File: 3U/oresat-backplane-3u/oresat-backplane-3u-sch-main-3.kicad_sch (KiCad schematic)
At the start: 30 parts

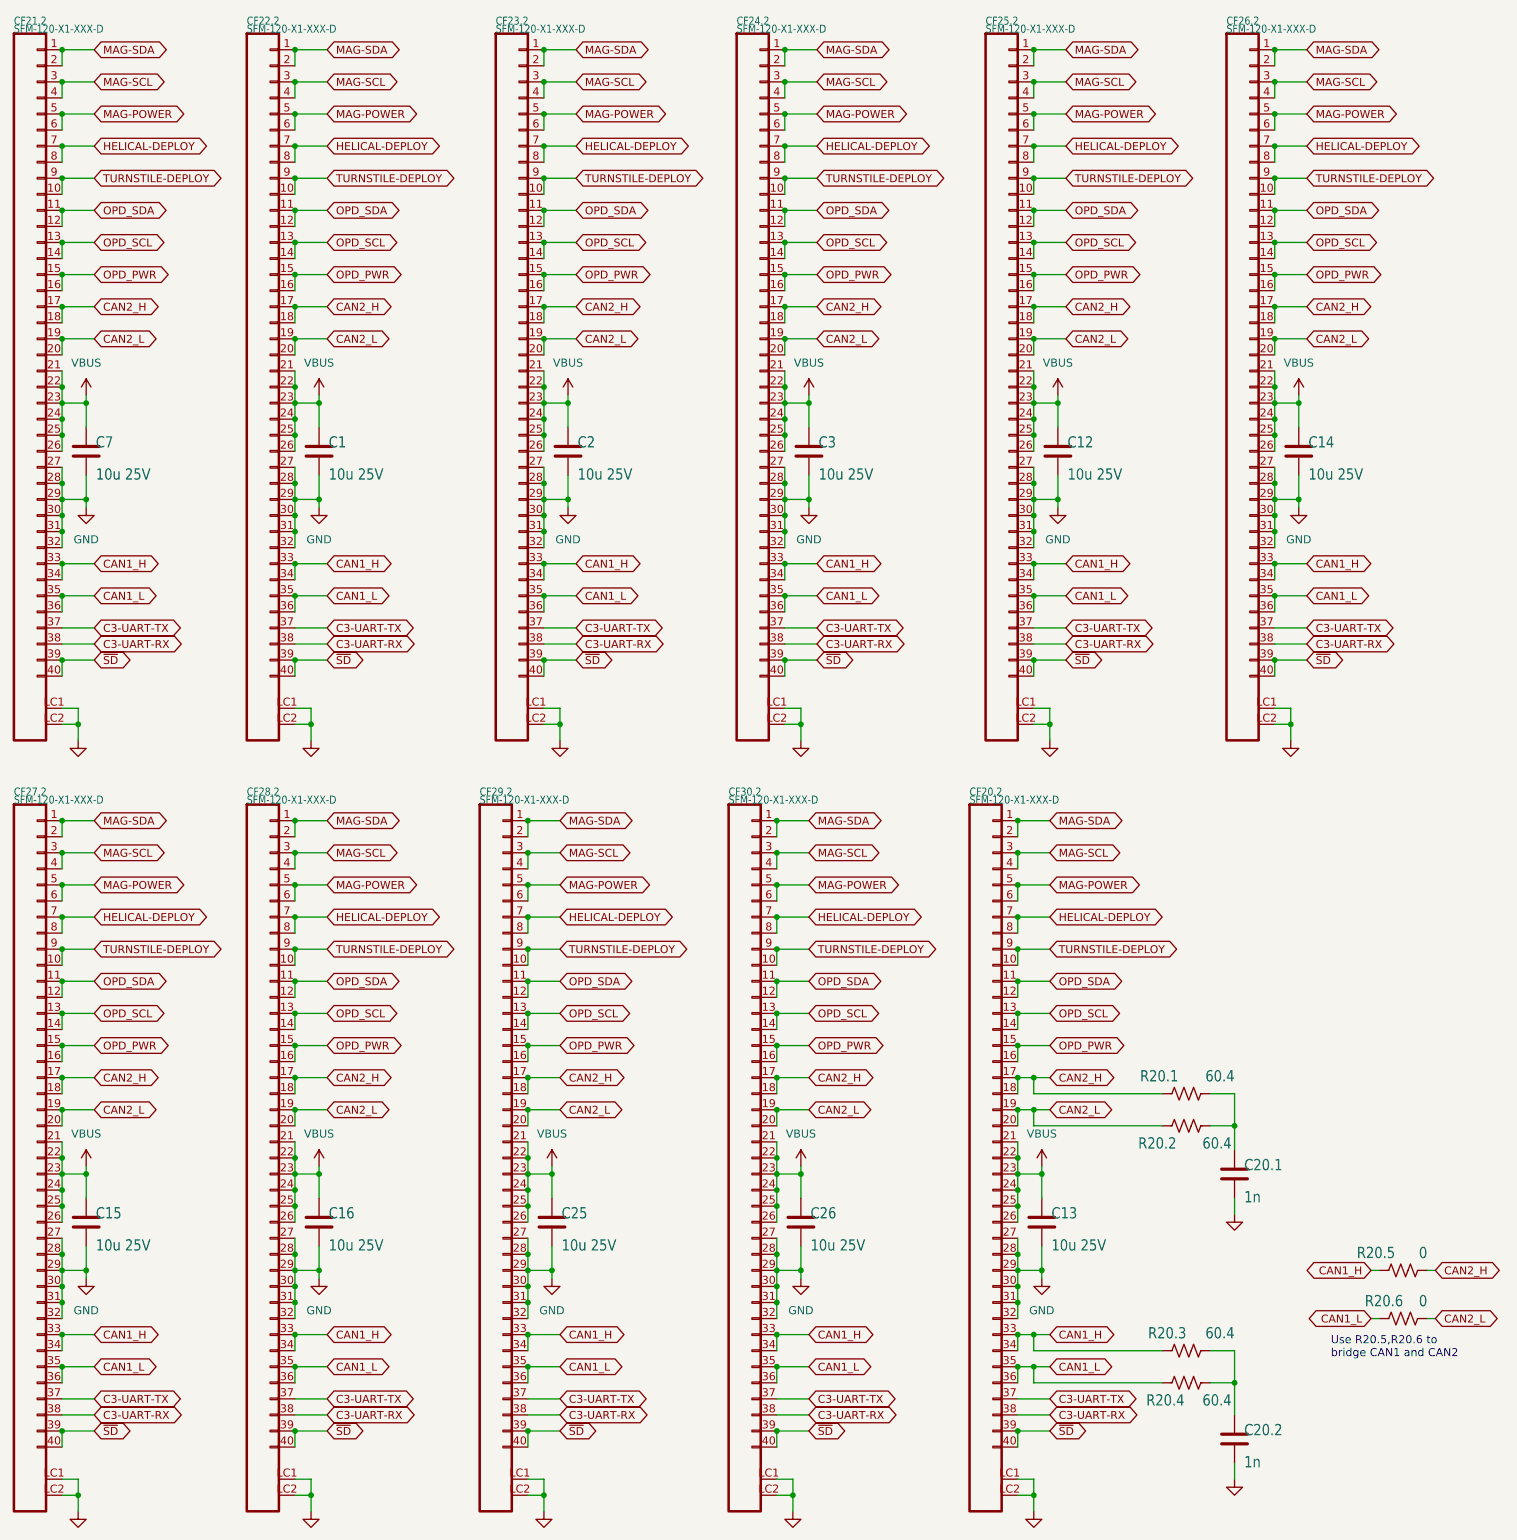
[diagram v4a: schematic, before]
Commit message: updated spare lines on schematic & began tracing
a little more than halfway through
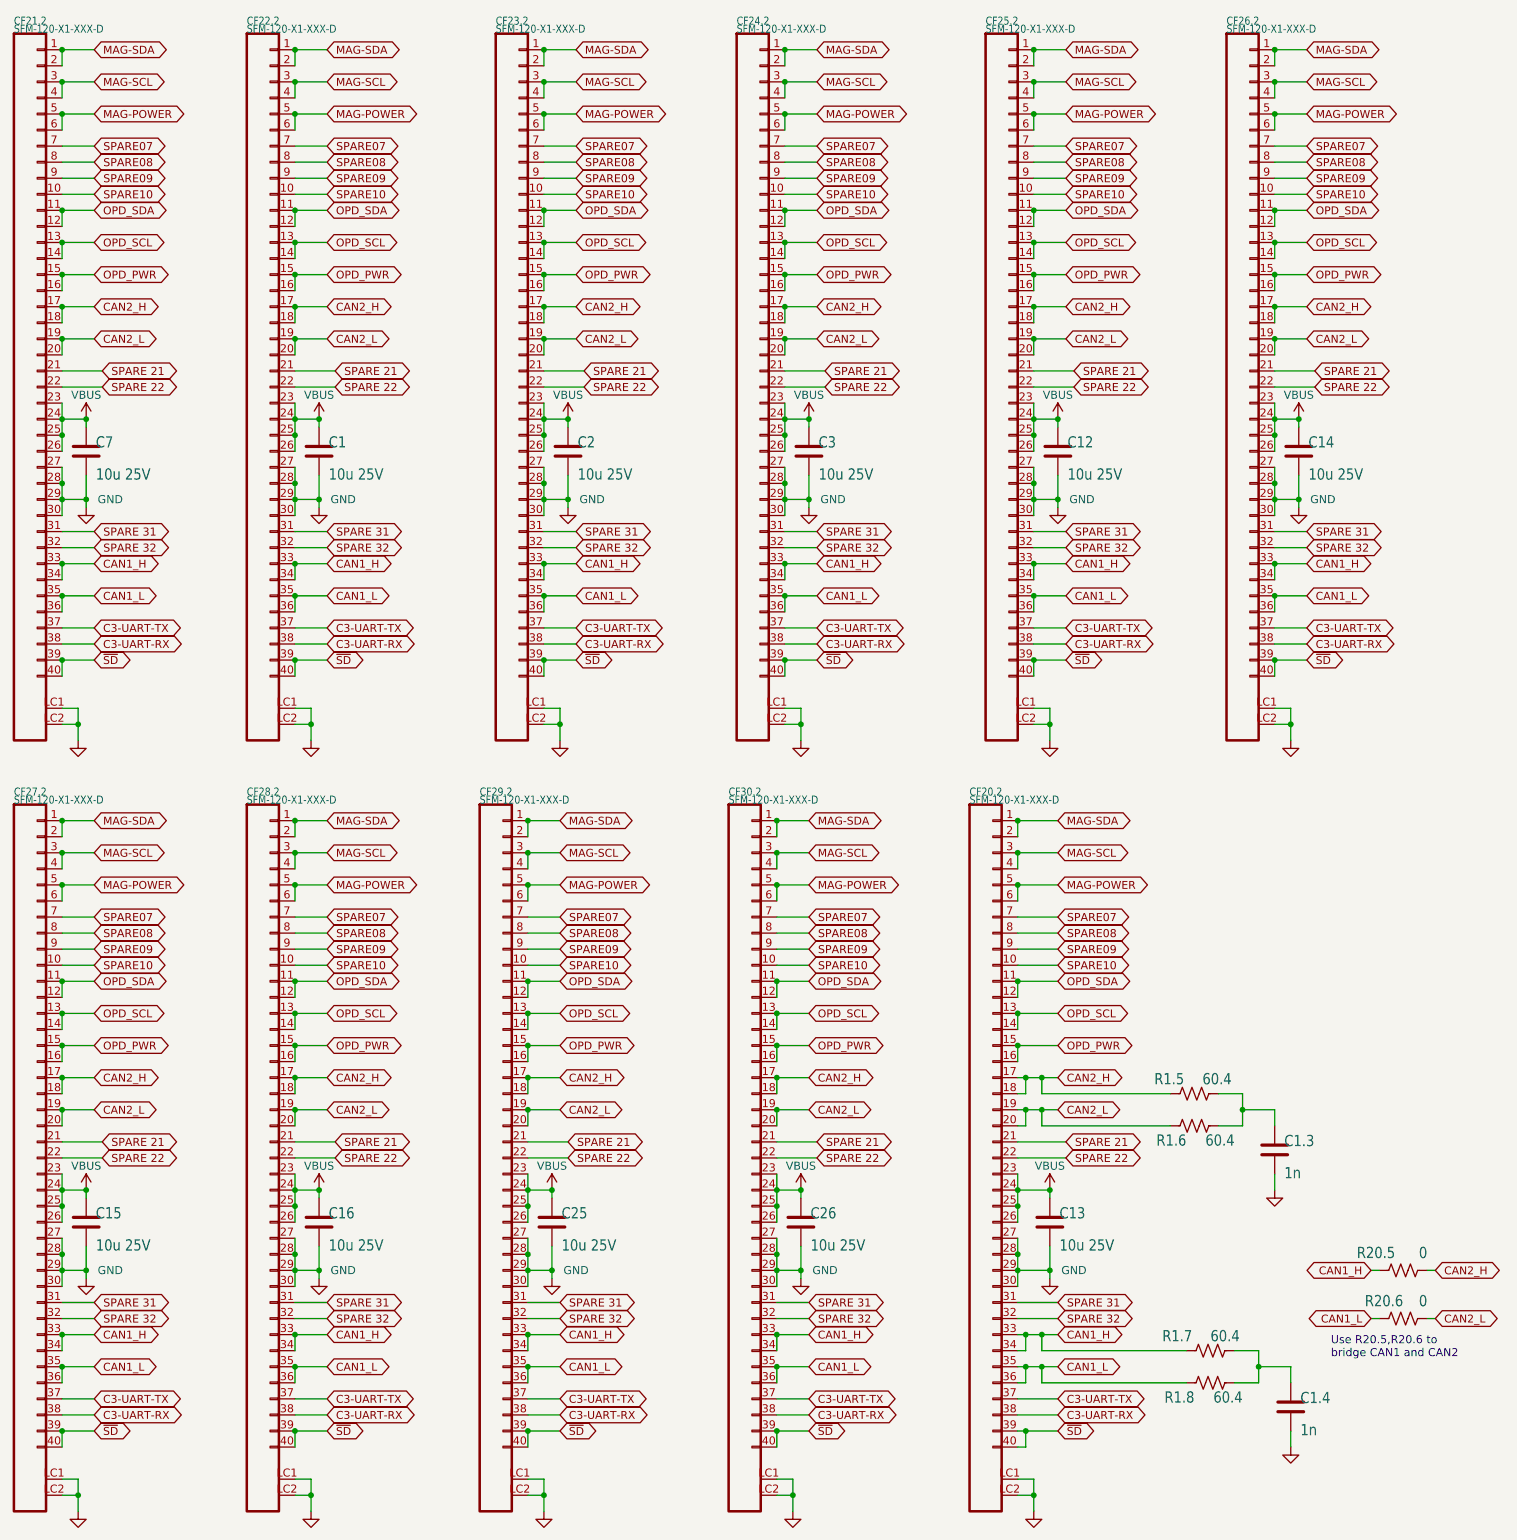
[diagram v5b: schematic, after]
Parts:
- removed C20.1, C20.2: 1n, oresat-passives:0603-C-NOSILK, symbol Device:C
- removed R20.1, R20.2, R20.3, R20.4: 60.4, Resistor_SMD:R_1206_3216Metric, symbol Device:R_US
- added C1.3, C1.4: 1n, oresat-passives:0603-C-NOSILK, symbol Device:C
- added R1.5, R1.6, R1.7, R1.8: 60.4, Resistor_SMD:R_1206_3216Metric, symbol Device:R_US
- C1, C12, C13, C14, C15, C16, C2, C25, C26, C3, C7: DIS (none) -> DigiKey; DPN (none) -> 587-3485-1-ND; MFR (none) -> Taiyo Yuden; MPN (none) -> TMK316AB7106KLHT
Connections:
- net CAN1_H: now also R1.7.2
- net CAN1_L: now also R1.8.1
- net CAN2_H: now also R1.5.2
- net CAN2_L: now also R1.6.1
- net GND: now also C1.3.2, C1.4.2; no longer CF20.2.31, CF20.2.32, CF21.2.31, CF21.2.32, CF22.2.31, CF22.2.32, CF23.2.31, CF23.2.32, CF24.2.31, CF24.2.32, CF25.2.31, CF25.2.32, CF26.2.31, CF26.2.32, CF27.2.31, CF27.2.32, CF28.2.31, CF28.2.32, CF29.2.31, CF29.2.32, CF30.2.31, CF30.2.32
- net VBUS: no longer CF20.2.21, CF20.2.22, CF21.2.21, CF21.2.22, CF22.2.21, CF22.2.22, CF23.2.21, CF23.2.22, CF24.2.21, CF24.2.22, CF25.2.21, CF25.2.22, CF26.2.21, CF26.2.22, CF27.2.21, CF27.2.22, CF28.2.21, CF28.2.22, CF29.2.21, CF29.2.22, CF30.2.21, CF30.2.22
- net HELICAL-DEPLOY renamed SPARE07
- net SPARE07: no longer CF20.2.8, CF21.2.8, CF22.2.8, CF23.2.8, CF24.2.8, CF25.2.8, CF26.2.8, CF27.2.8, CF28.2.8, CF29.2.8, CF30.2.8
- net TURNSTILE-DEPLOY renamed SPARE09
- net SPARE09: no longer CF20.2.10, CF21.2.10, CF22.2.10, CF23.2.10, CF24.2.10, CF25.2.10, CF26.2.10, CF27.2.10, CF28.2.10, CF29.2.10, CF30.2.10
- new net: C1.4.1, R1.7.1, R1.8.2
- new net: C1.3.1, R1.5.1, R1.6.2
- new net SPARE 21: CF20.2.21, CF21.2.21, CF22.2.21, CF23.2.21, CF24.2.21, CF25.2.21, CF26.2.21, CF27.2.21, CF28.2.21, CF29.2.21, CF30.2.21
- new net SPARE 22: CF20.2.22, CF21.2.22, CF22.2.22, CF23.2.22, CF24.2.22, CF25.2.22, CF26.2.22, CF27.2.22, CF28.2.22, CF29.2.22, CF30.2.22
- new net SPARE 31: CF20.2.31, CF21.2.31, CF22.2.31, CF23.2.31, CF24.2.31, CF25.2.31, CF26.2.31, CF27.2.31, CF28.2.31, CF29.2.31, CF30.2.31
- new net SPARE 32: CF20.2.32, CF21.2.32, CF22.2.32, CF23.2.32, CF24.2.32, CF25.2.32, CF26.2.32, CF27.2.32, CF28.2.32, CF29.2.32, CF30.2.32
- new net SPARE08: CF20.2.8, CF21.2.8, CF22.2.8, CF23.2.8, CF24.2.8, CF25.2.8, CF26.2.8, CF27.2.8, CF28.2.8, CF29.2.8, CF30.2.8
- new net SPARE10: CF20.2.10, CF21.2.10, CF22.2.10, CF23.2.10, CF24.2.10, CF25.2.10, CF26.2.10, CF27.2.10, CF28.2.10, CF29.2.10, CF30.2.10
